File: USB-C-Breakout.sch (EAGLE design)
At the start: 14 parts

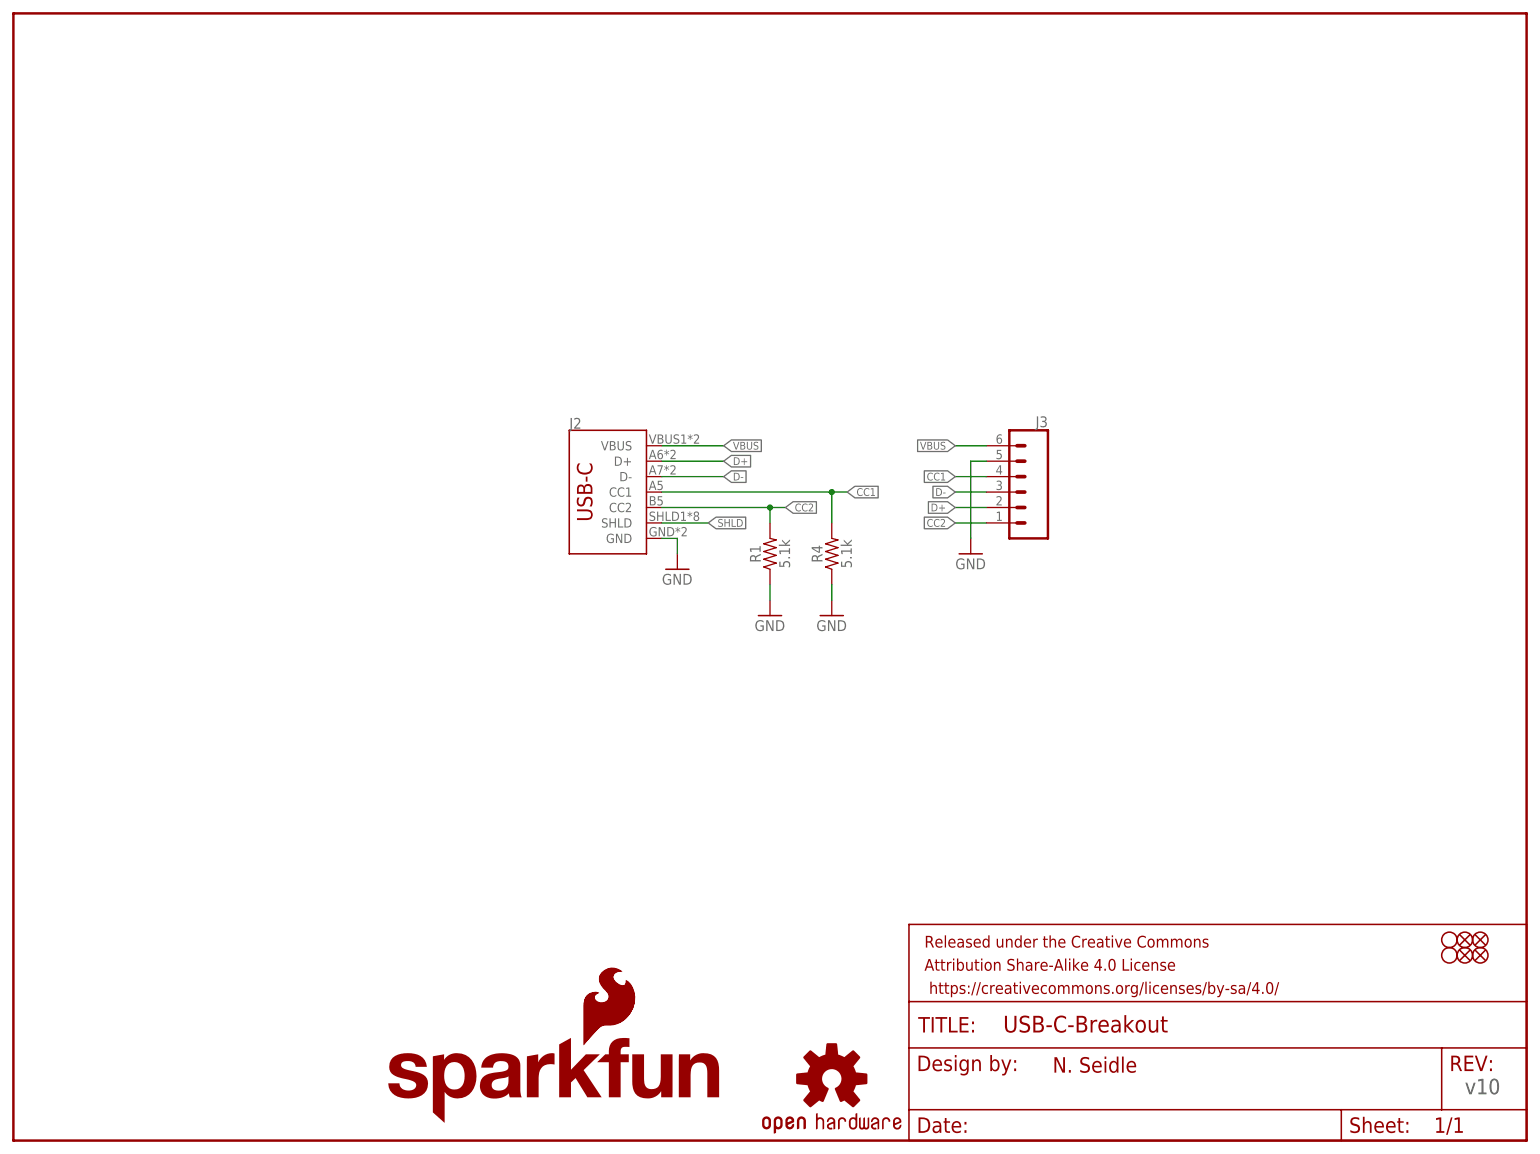
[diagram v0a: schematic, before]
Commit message: Updated library, tidied up schematic, deleted unneccesary files, and added readme
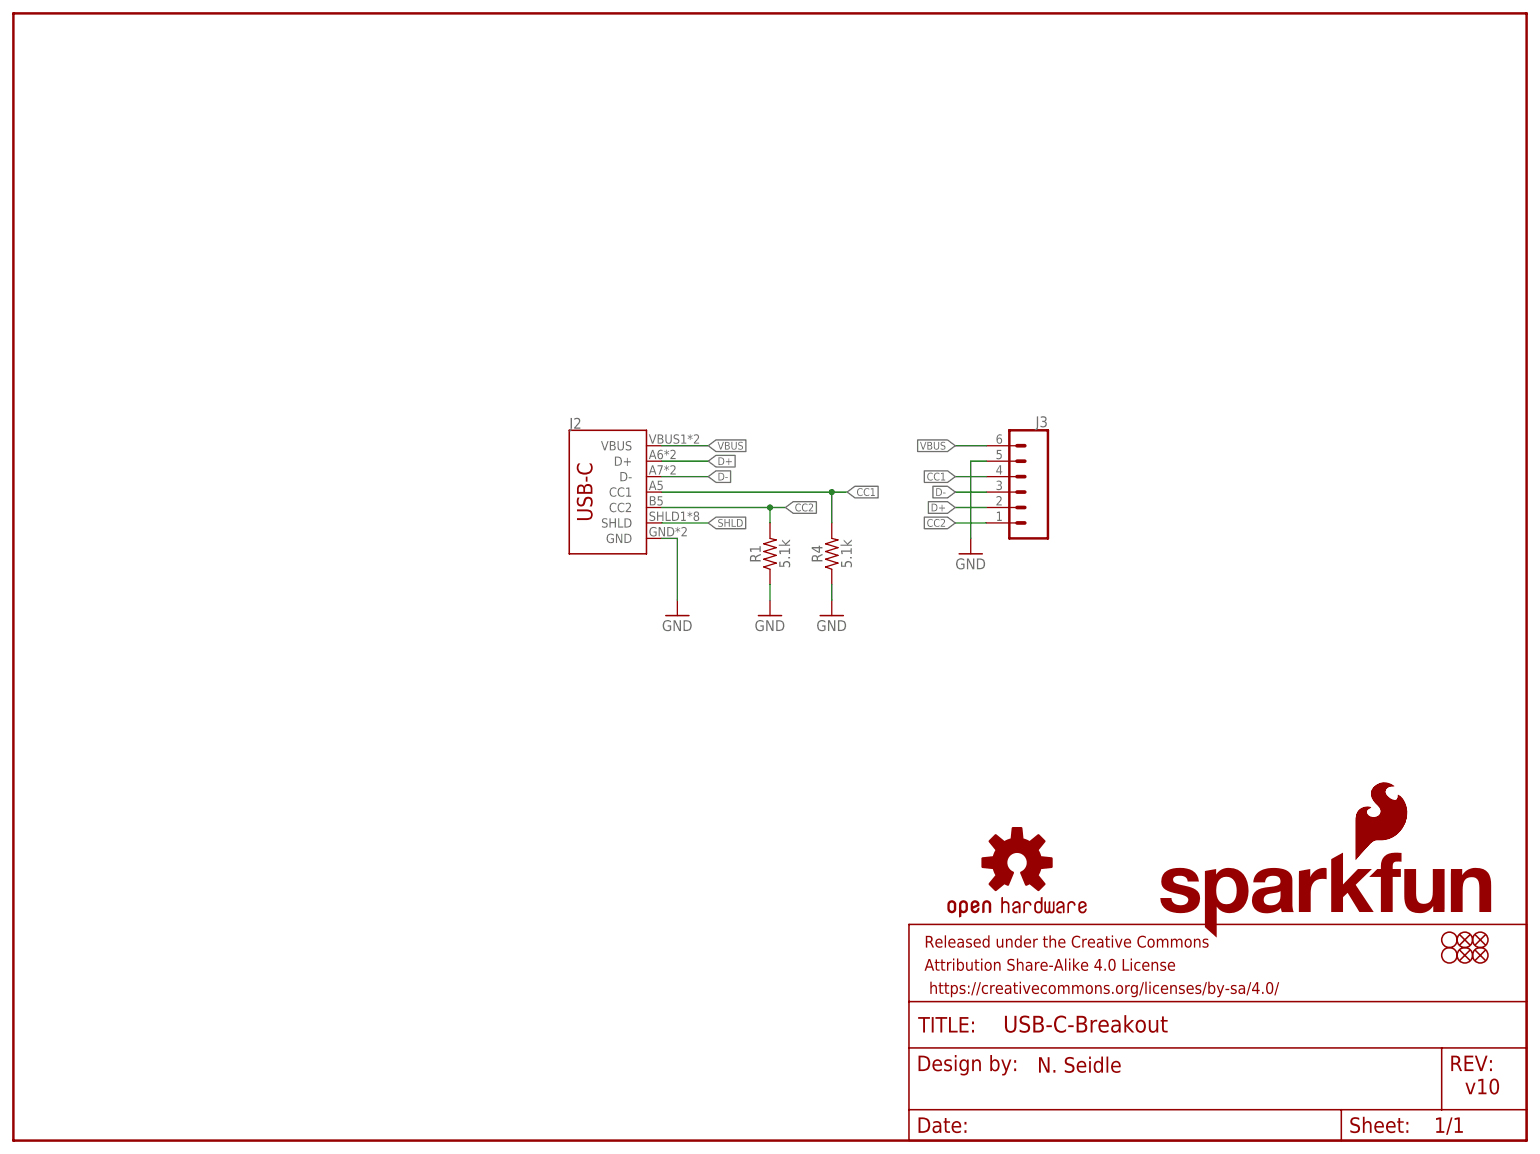
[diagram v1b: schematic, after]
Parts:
- J2: device USB-C:USB_C16PIN -> SparkFun-Connectors:USB_C16PIN
